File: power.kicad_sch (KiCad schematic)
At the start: 1 part

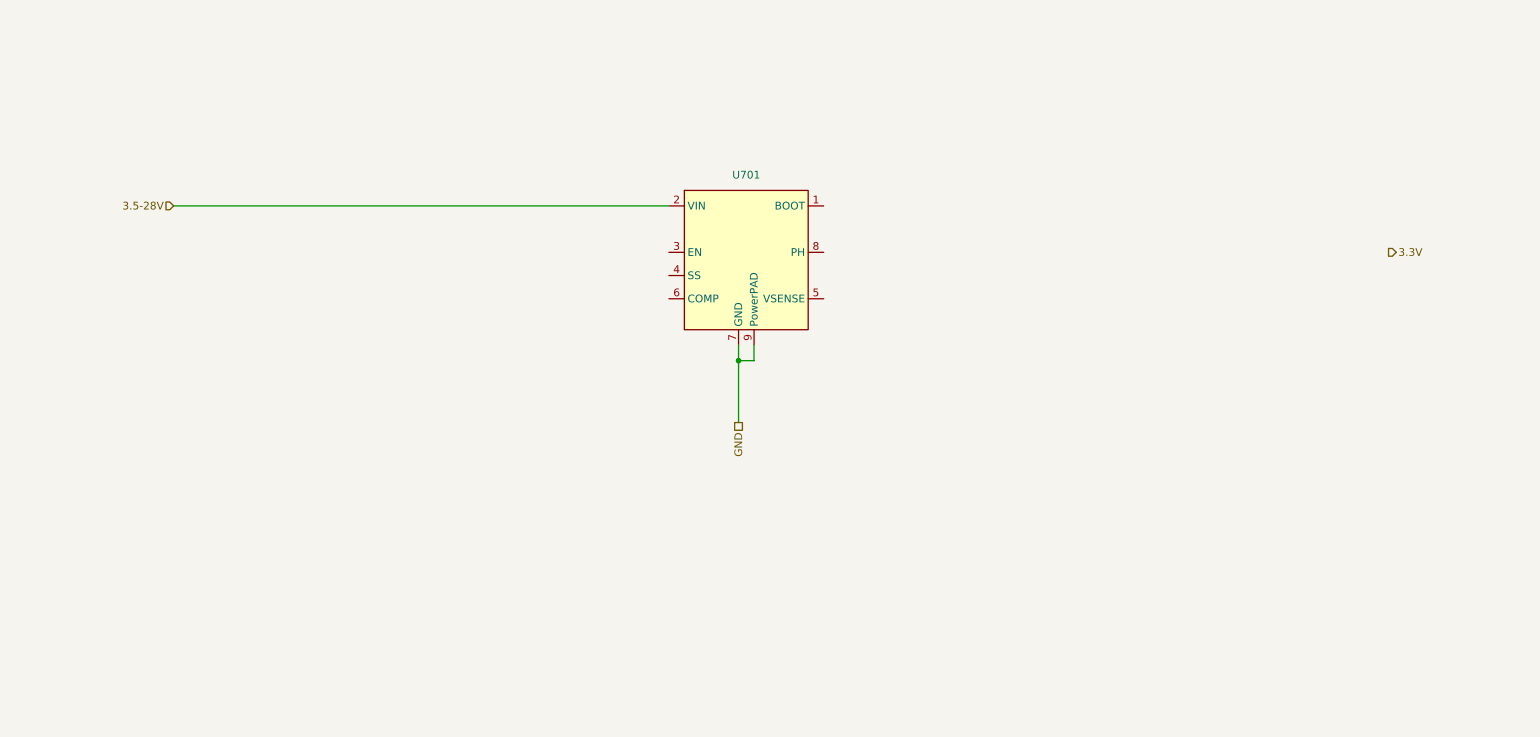
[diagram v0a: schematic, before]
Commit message: Add power management
And also some random stuff here and there
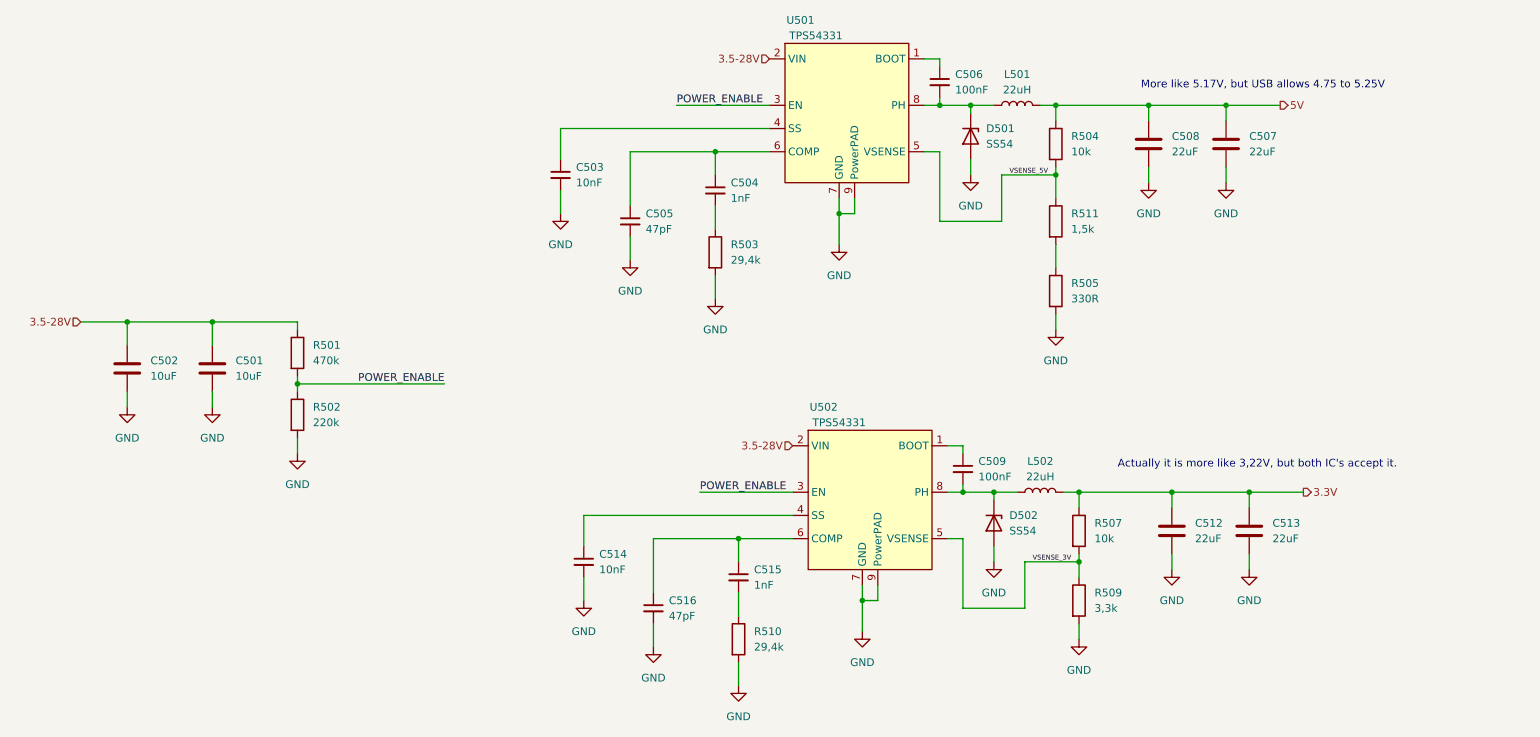
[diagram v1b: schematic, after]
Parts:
- removed U701: ~, Package_SO:SOIC-8-1EP_3.9x4.9mm_P1.27mm_EP2.29x3mm_ThermalVias, symbol fabian_power:TPS54331DR
- added C501, C502: 10uF, Capacitor_SMD:C_0805_2012Metric, symbol Device:C
- added C503, C514: 10nF, Resistor_SMD:R_0402_1005Metric, symbol Device:C_Small
- added C504, C515: 1nF, Resistor_SMD:R_0402_1005Metric, symbol Device:C_Small
- added C505, C516: 47pF, Resistor_SMD:R_0402_1005Metric, symbol Device:C_Small
- added C506, C509: 100nF, Resistor_SMD:R_0402_1005Metric, symbol Device:C_Small
- added C507, C508, C512, C513: 22uF, Capacitor_SMD:C_0603_1608Metric, symbol Device:C
- added D501, D502: SS54, Diode_SMD:D_SMA, symbol Device:D_Zener
- added L501, L502: 22uH, Inductors:YSPI0630A, symbol Device:L
- added R501: 470k, Resistor_SMD:R_0402_1005Metric, symbol Device:R
- added R502: 220k, Resistor_SMD:R_0402_1005Metric, symbol Device:R
- added R503, R510: 29,4k, Resistor_SMD:R_0402_1005Metric, symbol Device:R
- added R504, R507: 10k, Resistor_SMD:R_0402_1005Metric, symbol Device:R
- added R505: 330R, Resistor_SMD:R_0402_1005Metric, symbol Device:R
- added R509: 3,3k, Resistor_SMD:R_0402_1005Metric, symbol Device:R
- added R511: 1,5k, Resistor_SMD:R_0402_1005Metric, symbol Device:R
- added U501, U502: TPS54331, Package_SO:SOIC-8-1EP_3.9x4.9mm_P1.27mm_EP2.29x3mm_ThermalVias, symbol fabian_power:TPS54331DR
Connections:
- net 3.3V: now also C512.1, C513.1, L502.2, R507.1
- net 3.5-28V: now also C501.1, C502.1, R501.1, U501.2 (VIN), U502.2 (VIN)
- net GND: now also C501.2, C502.2, C503.2, C505.2, C507.2, C508.2, C512.2, C513.2, C514.2, C516.2, D501.2 (A), D502.2 (A), R502.2, R503.2, R505.2, R509.2, R510.2, U501.7 (GND), U501.9 (PowerPAD), U502.7 (GND), U502.9 (PowerPAD)
- new net: C504.1, C505.1, U501.6 (COMP)
- new net: C504.2, R503.1
- new net: C515.1, C516.1, U502.6 (COMP)
- new net: C514.1, U502.4 (SS)
- new net: C515.2, R510.1
- new net: C509.2, D502.1 (K), L502.1, U502.8 (PH)
- new net: C506.1, U501.1 (BOOT)
- new net: C506.2, D501.1 (K), L501.1, U501.8 (PH)
- new net: C509.1, U502.1 (BOOT)
- new net: C503.1, U501.4 (SS)
- new net: R505.1, R511.2
- new net 5V: C507.1, C508.1, L501.2, R504.1
- new net POWER_ENABLE: R501.2, R502.1, U501.3 (EN), U502.3 (EN)
- new net VSENSE_3V: R507.2, R509.1, U502.5 (VSENSE)
- new net VSENSE_5V: R504.2, R511.1, U501.5 (VSENSE)
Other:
- note added: "Actually it is more like 3,22V, but both IC's accept it."
- note added: "More like 5.17V, but USB allows 4.75 to 5.25V"

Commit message: Refine connectors and overall shape
Replace USB connectors, because of availability.
Use available barrel jack and USB-C connector instead of generic ones.
Update 3D Models

Refine rough placement of parts and board outline
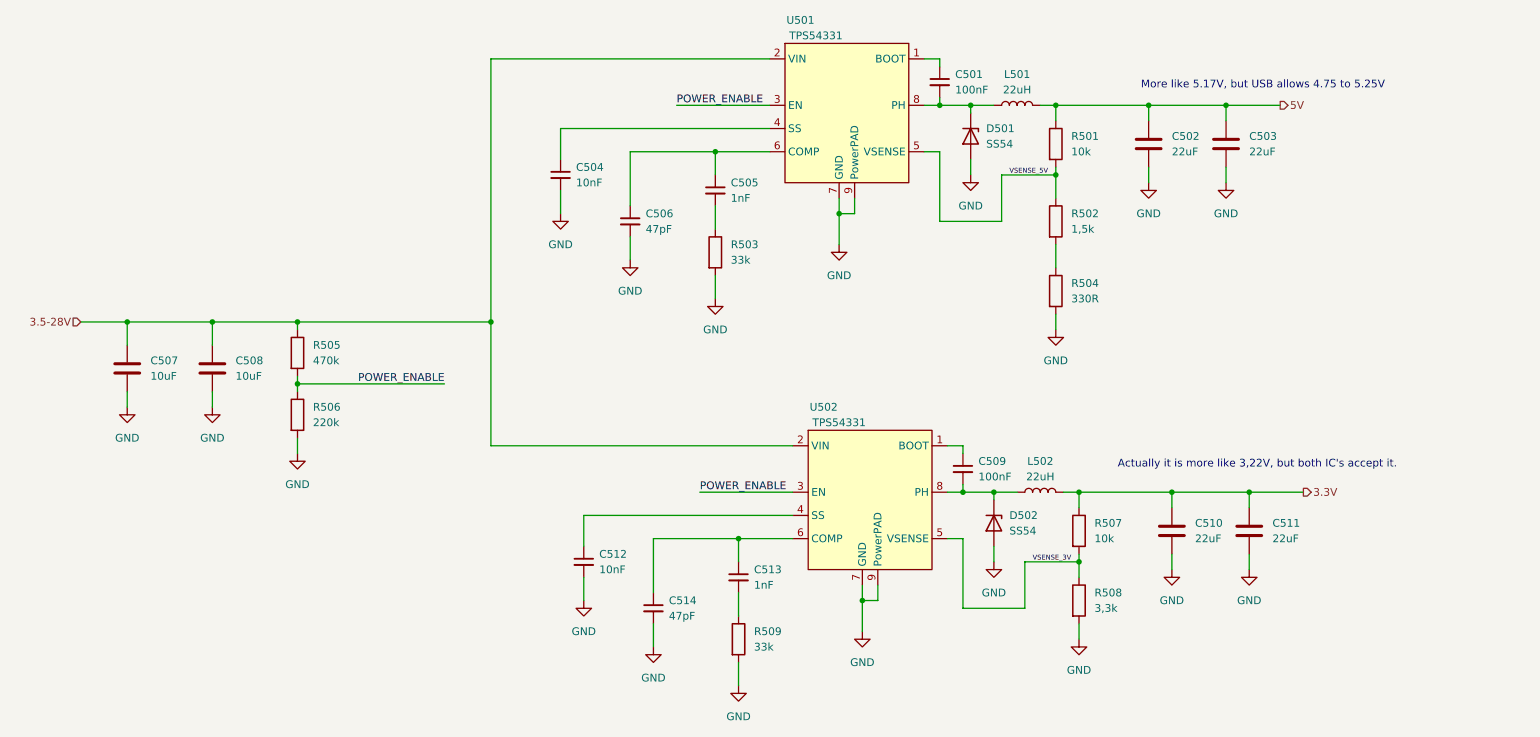
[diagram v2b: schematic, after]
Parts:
- C501: renamed from C506; footprint Resistor_SMD:R_0402_1005Metric -> Capacitor_SMD:C_0402_1005Metric; LCSC# (none) -> C307331
- C504: renamed from C503; footprint Resistor_SMD:R_0402_1005Metric -> Capacitor_SMD:C_0402_1005Metric; LCSC# (none) -> C15195
- C505: renamed from C504; footprint Resistor_SMD:R_0402_1005Metric -> Capacitor_SMD:C_0402_1005Metric; LCSC# (none) -> C1523
- C506: renamed from C505; footprint Resistor_SMD:R_0402_1005Metric -> Capacitor_SMD:C_0402_1005Metric; LCSC# (none) -> C1567
- C507: renamed from C502; MPN (none) -> 50V 10uF
- C509: footprint Resistor_SMD:R_0402_1005Metric -> Capacitor_SMD:C_0402_1005Metric; LCSC# (none) -> C307331
- C512: renamed from C514; footprint Resistor_SMD:R_0402_1005Metric -> Capacitor_SMD:C_0402_1005Metric; LCSC# (none) -> C15195
- C513: renamed from C515; footprint Resistor_SMD:R_0402_1005Metric -> Capacitor_SMD:C_0402_1005Metric; LCSC# (none) -> C1523
- C514: renamed from C516; footprint Resistor_SMD:R_0402_1005Metric -> Capacitor_SMD:C_0402_1005Metric; LCSC# (none) -> C1567
- R502: renamed from R511; MPN (none) -> 1,5k
- R503: value 29,4k -> 33k; LCSC# (none) -> C25779; MPN (none) -> 33k
- R506: renamed from R502; MPN (none) -> 220k
- R508: renamed from R509; LCSC# (none) -> C25890; MPN (none) -> 3,3k
- R509: renamed from R510; value 29,4k -> 33k; LCSC# (none) -> C25779; MPN (none) -> 33k
- U501, U502: MPN TPS54331 -> TPS54331DDA
- renumbered C508 to C502, C507 to C503, C501 to C508, C512 to C510, C513 to C511, R504 to R501, R505 to R504, R501 to R505

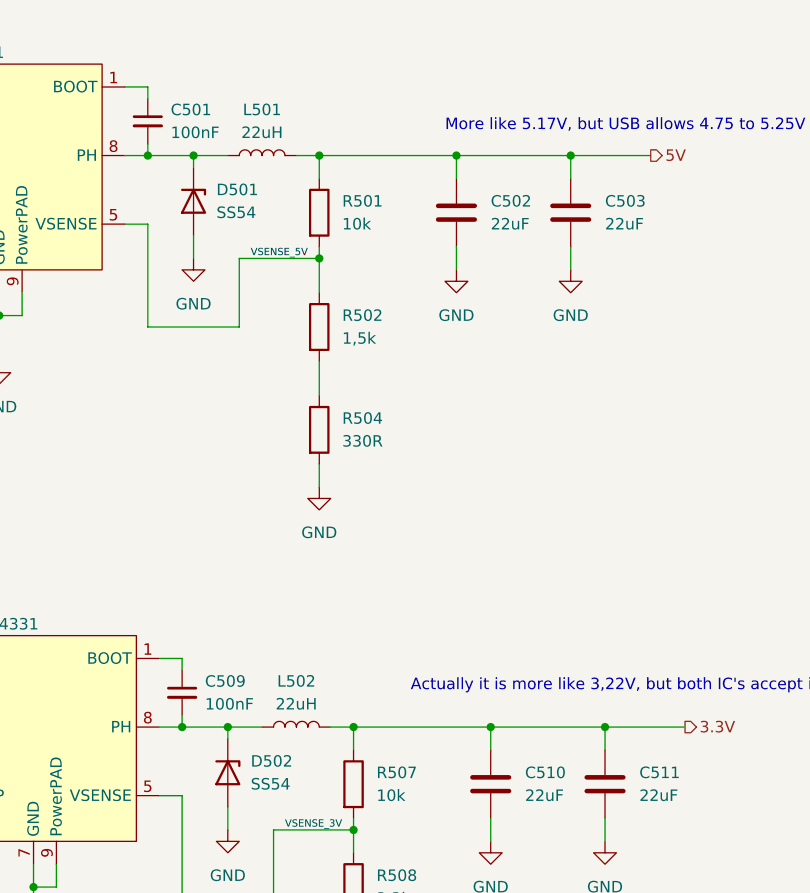
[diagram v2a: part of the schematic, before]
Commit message: Finish first routing
Routed everything, so that the DRC and ERC do not show anything.
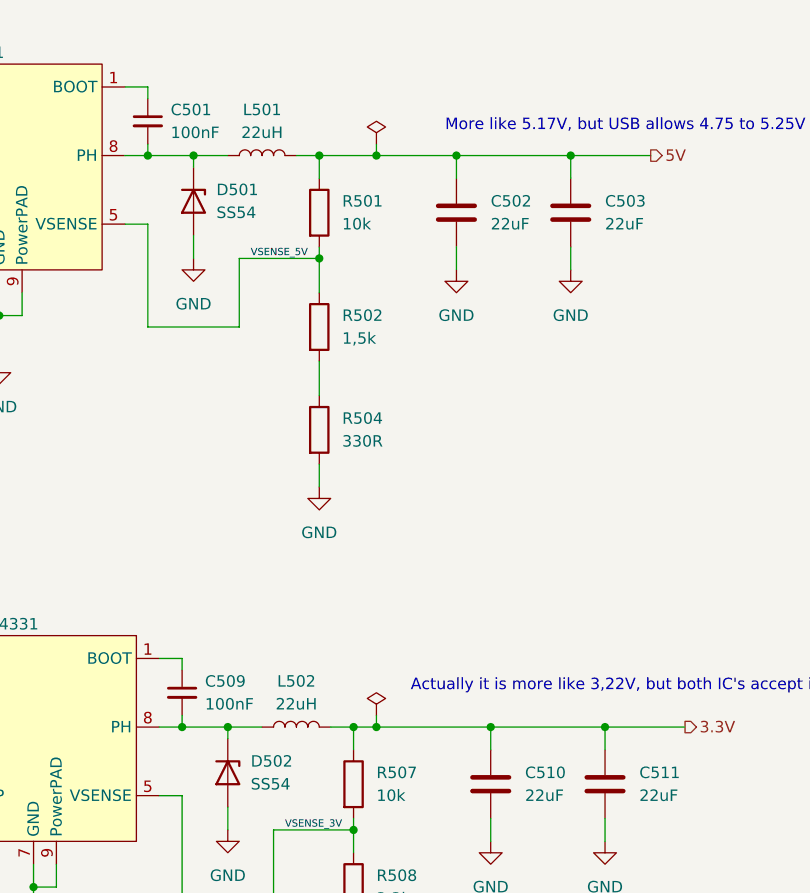
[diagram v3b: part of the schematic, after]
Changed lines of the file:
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@@
     (company "Fabian Pflug")
   )
+  (junction (at 200.66 57.15) (diameter 0) (color 0 0 0 0)
+  )
   (junction (at 198.12 120.65) (diameter 0) (color 0 0 0 0)
   )
@@
   (junction (at 69.85 102.87) (diameter 0) (color 0 0 0 0)
   )
+  (junction (at 200.66 120.65) (diameter 0) (color 0 0 0 0)
+  )
   (junction (at 184.15 120.65) (diameter 0) (color 0 0 0 0)
   )
@@
     (stroke (width 0) (type default))
   )
-  (wire (pts (xy 198.12 120.65) (xy 213.36 120.65))
+  (wire (pts (xy 200.66 119.38) (xy 200.66 120.65))
+    (stroke (width 0) (type default))
+  )
+  (wire (pts (xy 198.12 120.65) (xy 200.66 120.65))
     (stroke (width 0) (type default))
   )
@@
     (stroke (width 0) (type default))
   )
-  (wire (pts (xy 194.31 57.15) (xy 209.55 57.15))
+  (wire (pts (xy 194.31 57.15) (xy 200.66 57.15))
     (stroke (width 0) (type default))
   )
@@
     (stroke (width 0) (type default))
   )
+  (wire (pts (xy 200.66 120.65) (xy 213.36 120.65))
+    (stroke (width 0) (type default))
+  )
   (wire (pts (xy 69.85 102.87) (xy 69.85 104.14))
     (stroke (width 0) (type default))
@@
     (stroke (width 0) (type default))
   )
+  (wire (pts (xy 200.66 55.88) (xy 200.66 57.15))
+    (stroke (width 0) (type default))
+  )
   (wire (pts (xy 124.46 73.66) (xy 124.46 64.77))
     (stroke (width 0) (type default))
@@
   )
   (wire (pts (xy 184.15 120.65) (xy 187.96 120.65))
+    (stroke (width 0) (type default))
+  )
+  (wire (pts (xy 200.66 57.15) (xy 209.55 57.15))
     (stroke (width 0) (type default))
   )
@@
     )
   )
+  (symbol (lib_id "power:PWR_FLAG") (at 200.66 119.38 0) (unit 1)
+    (in_bom yes) (on_board yes) (dnp no) (fields_autoplaced)
+    (property "Reference" "#FLG0502" (at 200.66 117.475 0)
+      (effects (font (size 1.27 1.27)) hide)
+    )
+    (property "Value" "PWR_FLAG" (at 200.66 114.3 0)
+      (effects (font (size 1.27 1.27)) hide)
+    )
+    (property "Footprint" "" (at 200.66 119.38 0)
+      (effects (font (size 1.27 1.27)) hide)
+    )
+    (property "Datasheet" "~" (at 200.66 119.38 0)
+      (effects (font (size 1.27 1.27)) hide)
+    )
+    (pin "1")
+    (instances
+      (project "usb-hub"
+        (path "/b46faf57-adcb-44f4-ac46-f905e4e8952b/e35210e8-490f-4665-90b3-f7b898938663"
+          (reference "#FLG0502") (unit 1)
+        )
+      )
+    )
+  )
   (symbol (lib_id "Device:C_Small") (at 128.27 139.7 0) (unit 1)
     (in_bom yes) (on_board yes) (dnp no) (fields_autoplaced)
@@
         )
       )
+    )
+  )
+  (symbol (lib_id "power:PWR_FLAG") (at 200.66 55.88 0) (unit 1)
+    (in_bom yes) (on_board yes) (dnp no) (fields_autoplaced)
+    (property "Reference" "#FLG0501" (at 200.66 53.975 0)
+      (effects (font (size 1.27 1.27)) hide)
+    )
+    (property "Value" "PWR_FLAG" (at 200.66 50.8 0)
+      (effects (font (size 1.27 1.27)) hide)
+    )
+    (property "Footprint" "" (at 200.66 55.88 0)
+      (effects (font (size 1.27 1.27)) hide)
+    )
+    (property "Datasheet" "~" (at 200.66 55.88 0)
+      (effects (font (size 1.27 1.27)) hide)
+    )
+    (pin "1")
+    (instances
+      (project "usb-hub"
+        (path "/b46faf57-adcb-44f4-ac46-f905e4e8952b/e35210e8-490f-4665-90b3-f7b898938663"
+          (reference "#FLG0501") (unit 1)
+        )
+      )

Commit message: Update to new enviroment
Kicad 8 & global symbols and footprint library
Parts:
- L501, L502: footprint Inductors:YSPI0630A -> g-Inductors:YSPI0630A
- U501, U502: symbol fabian_power:TPS54331DR -> g-power:TPS54331DR; MPN TPS54331DDA -> TPS54331
